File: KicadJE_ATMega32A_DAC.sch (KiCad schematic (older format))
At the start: 97 parts

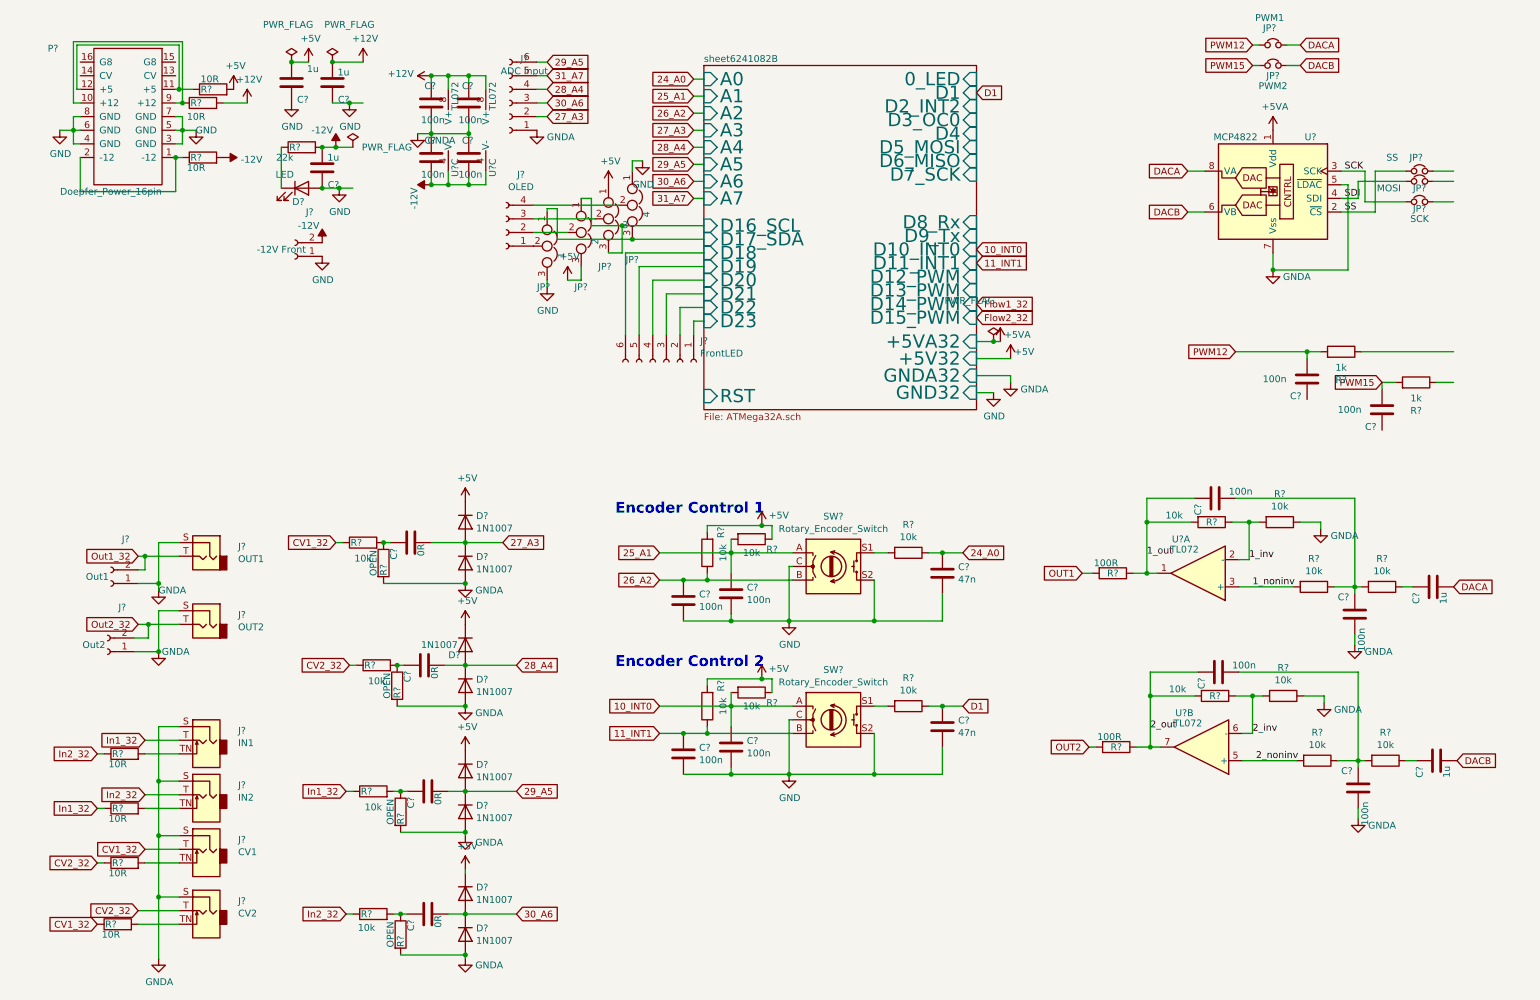
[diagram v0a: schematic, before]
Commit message: annotate dac
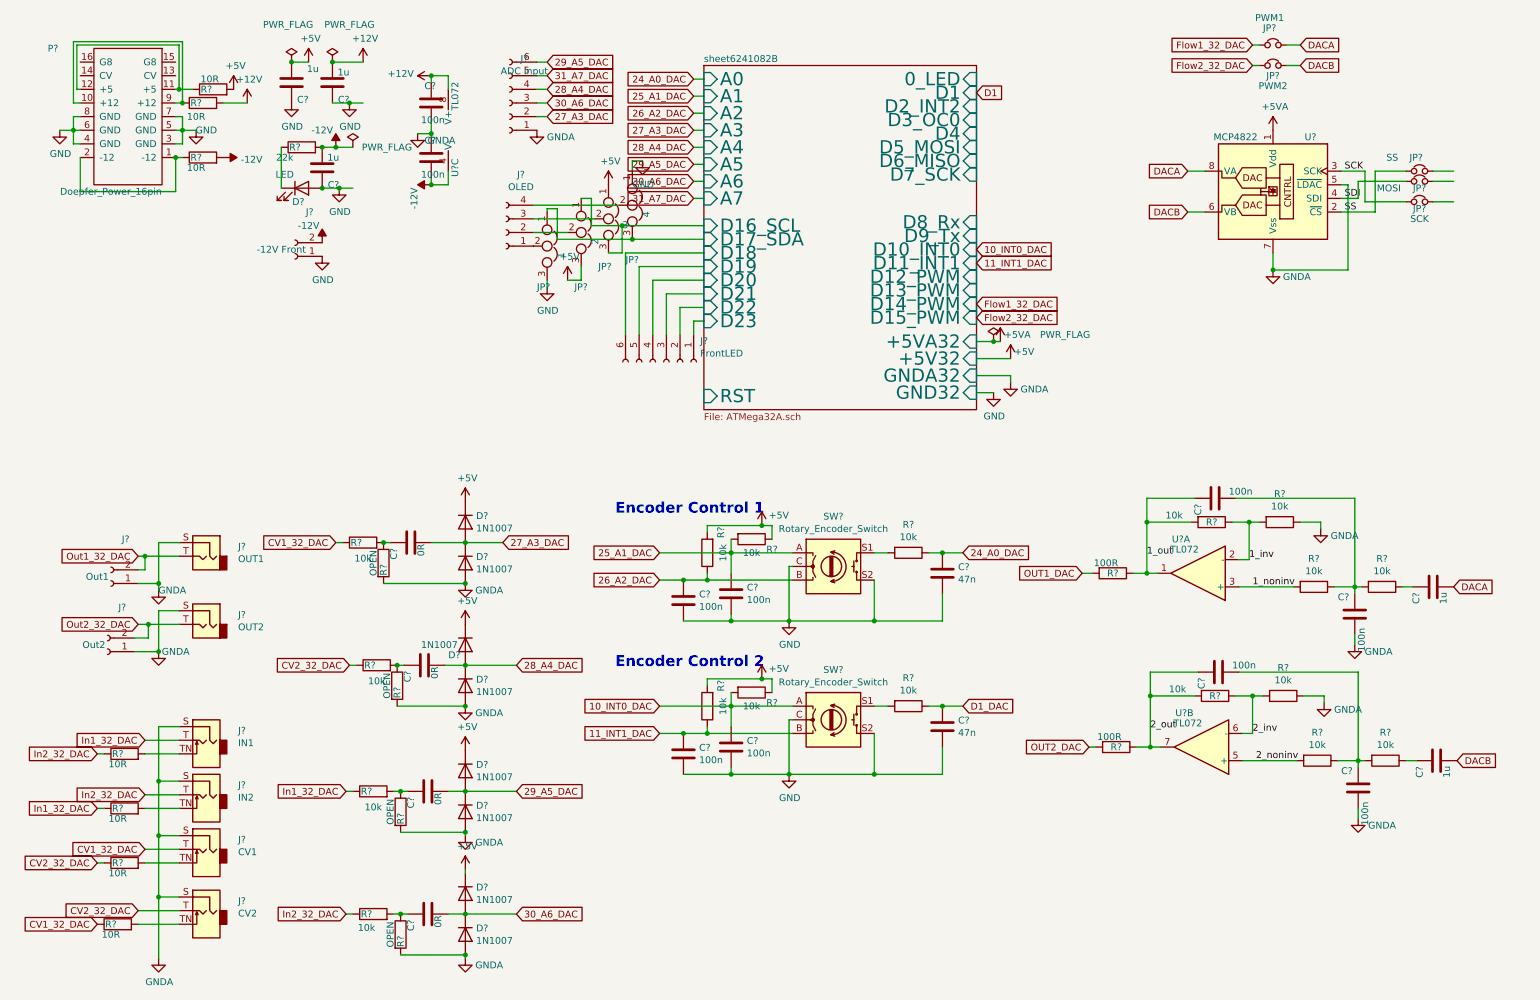
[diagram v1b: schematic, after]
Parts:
- removed C212, C213: 100n, Capacitor_SMD:C_0805_2012Metric_Pad1.15x1.40mm_HandSolder, symbol Device:C
- removed C? (x2): 100n, AJ:C_0805_AJ, symbol Device:C
- removed R218, R223: 1k, Resistor_SMD:R_0805_2012Metric_Pad1.15x1.40mm_HandSolder, symbol Device:R
- removed U?: TL072, AJ:AJ_SO-8_5.3x6.2mm_P1.27mm, symbol Amplifier_Operational:TL072
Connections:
- net D1: no longer C?.1, R?.1
- net 10_INT0 renamed 10_INT0_DAC
- net 11_INT1 renamed 11_INT1_DAC
- net 24_A0 renamed 24_A0_DAC
- net 25_A1 renamed 25_A1_DAC
- net 26_A2 renamed 26_A2_DAC
- net 27_A3 renamed 27_A3_DAC
- net 28_A4 renamed 28_A4_DAC
- net 29_A5 renamed 29_A5_DAC
- net 30_A6 renamed 30_A6_DAC
- net 31_A7 renamed 31_A7_DAC
- net CV1_32 renamed CV1_32_DAC
- net CV2_32 renamed CV2_32_DAC
- net In1_32 renamed In1_32_DAC
- net In2_32 renamed In2_32_DAC
- net OUT1 renamed OUT1_DAC
- net OUT2 renamed OUT2_DAC
- net Out1_32 renamed Out1_32_DAC
- net Out2_32 renamed Out2_32_DAC
- net PWM12 renamed Flow1_32_DAC
- net PWM15 renamed Flow2_32_DAC
- new net D1_DAC: C?.1, R?.1

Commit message: footprints dac
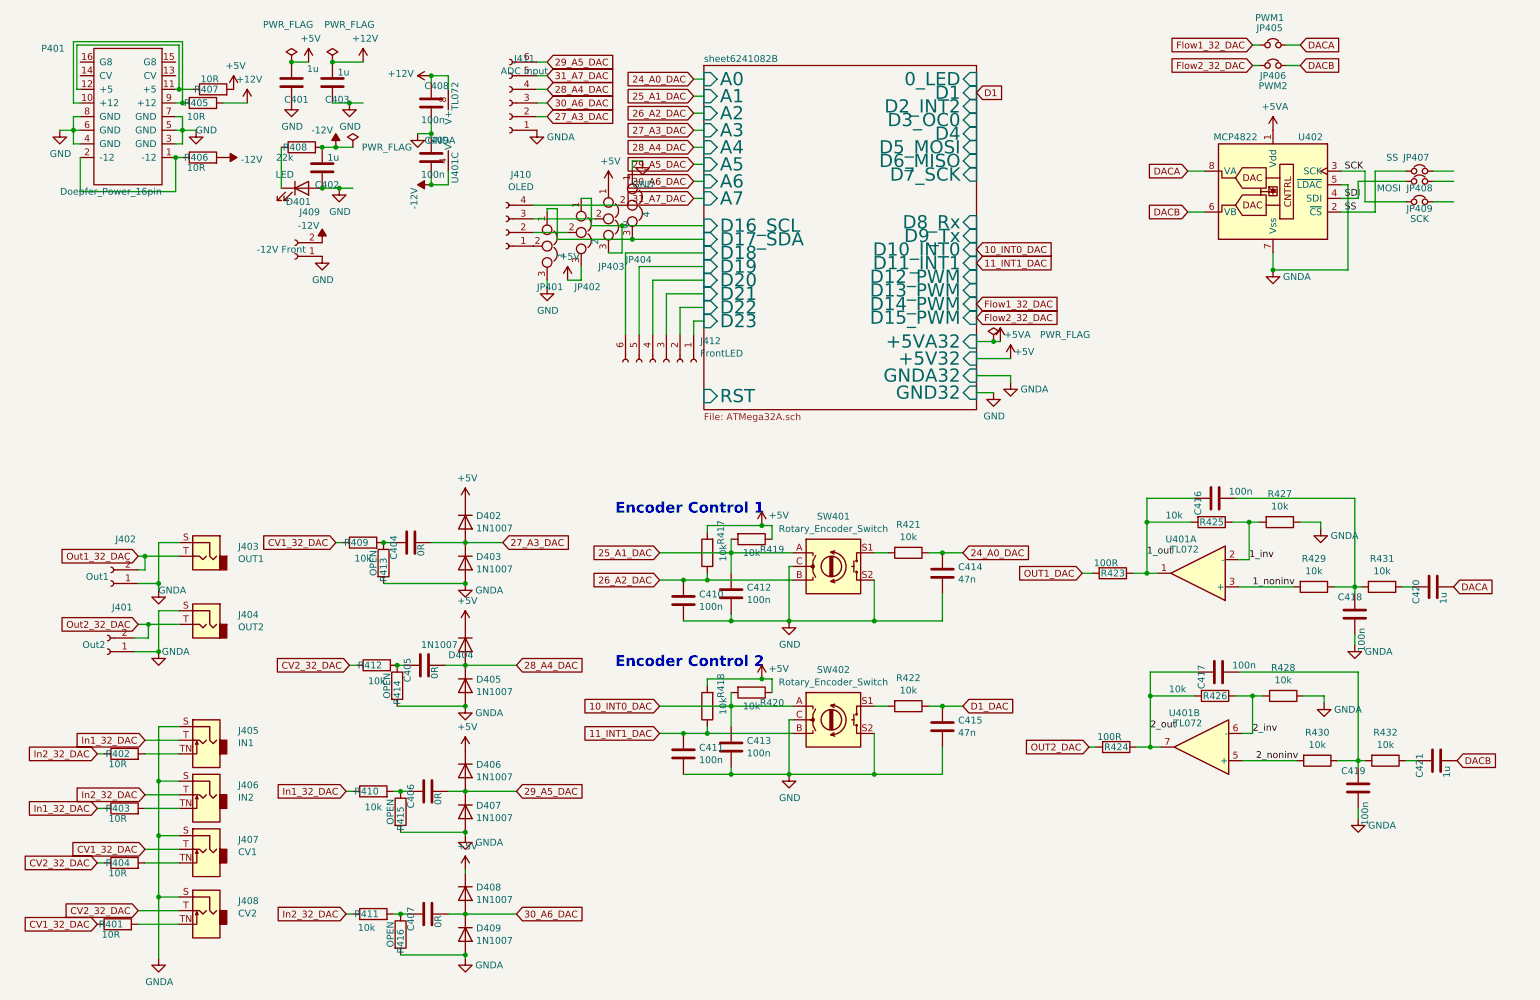
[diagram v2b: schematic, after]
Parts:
- C206, C208, C209, C211: footprint Capacitor_SMD:C_0805_2012Metric_Pad1.15x1.40mm_HandSolder -> AJ:C_0805_AJ
- C207, C210: footprint Capacitor_SMD:C_1206_3216Metric_Pad1.42x1.75mm_HandSolder -> AJ:C_0805_AJ
- R205, R206, R207, R208, R209, R211, R212, R213, R214, R215: footprint Resistor_SMD:R_0805_2012Metric_Pad1.15x1.40mm_HandSolder -> AJ:R_0805_AJ
- gave numbers to parts that had none: 72

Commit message: Components placed
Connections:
- net Out1_32_DAC is gone; now on net OUT1_DAC: J402.2 (Pin_2), J403.T
- net Out2_32_DAC is gone; now on net OUT2_DAC: J401.2 (Pin_2), J404.T
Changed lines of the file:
@@
 Wire Wire Line
 	1200 4975 1275 4975
-Text GLabel 1200 4475 0    50   Input ~ 0
-Out1_32_DAC
-Text GLabel 1200 4975 0    50   Input ~ 0
-Out2_32_DAC
 $Comp
 L power:GNDA #PWR?
@@
 Text GLabel 9375 875  0    50   Input ~ 0
 Flow2_32_DAC
+Text GLabel 1200 4475 0    50   Input ~ 0
+OUT1_DAC
+Text GLabel 1200 4975 0    50   Input ~ 0
+OUT2_DAC
 $EndSCHEMATC

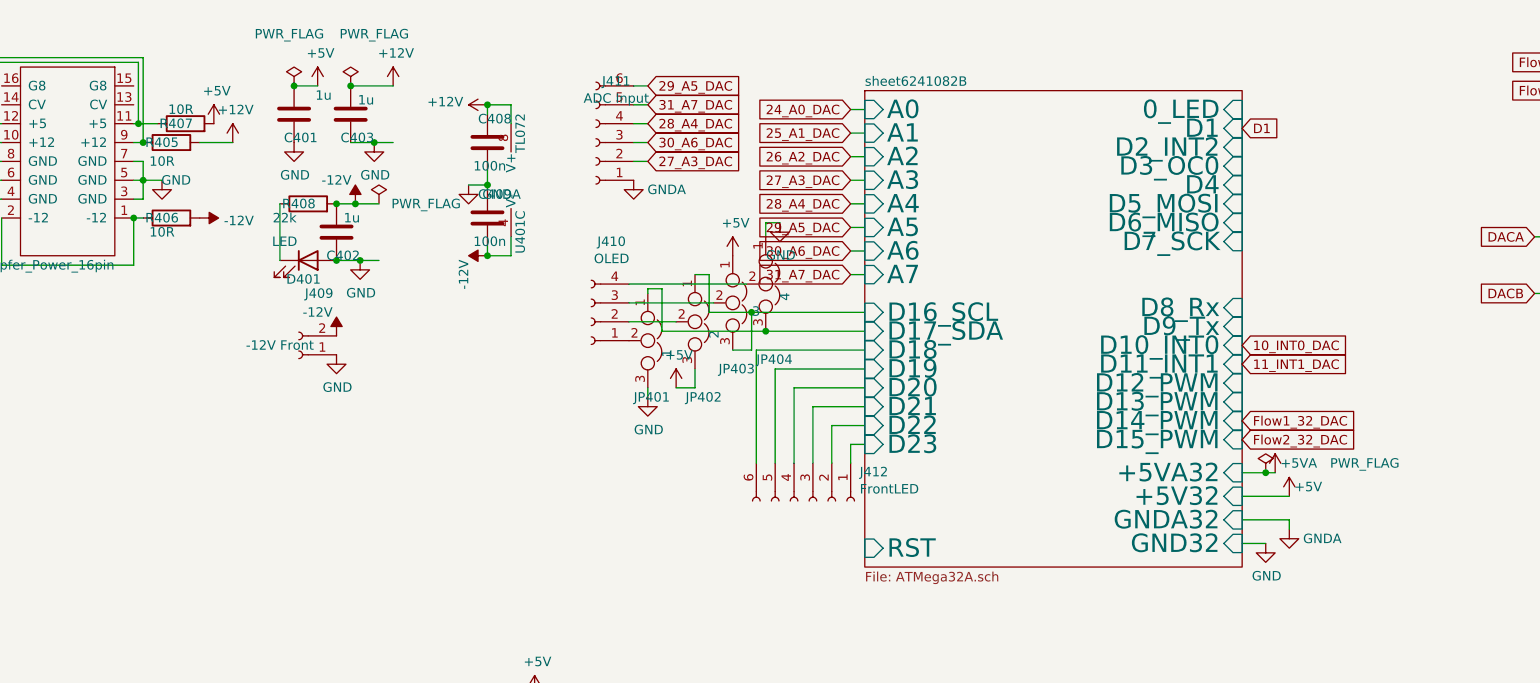
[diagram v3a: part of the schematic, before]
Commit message: Wiring DAC board - initiated
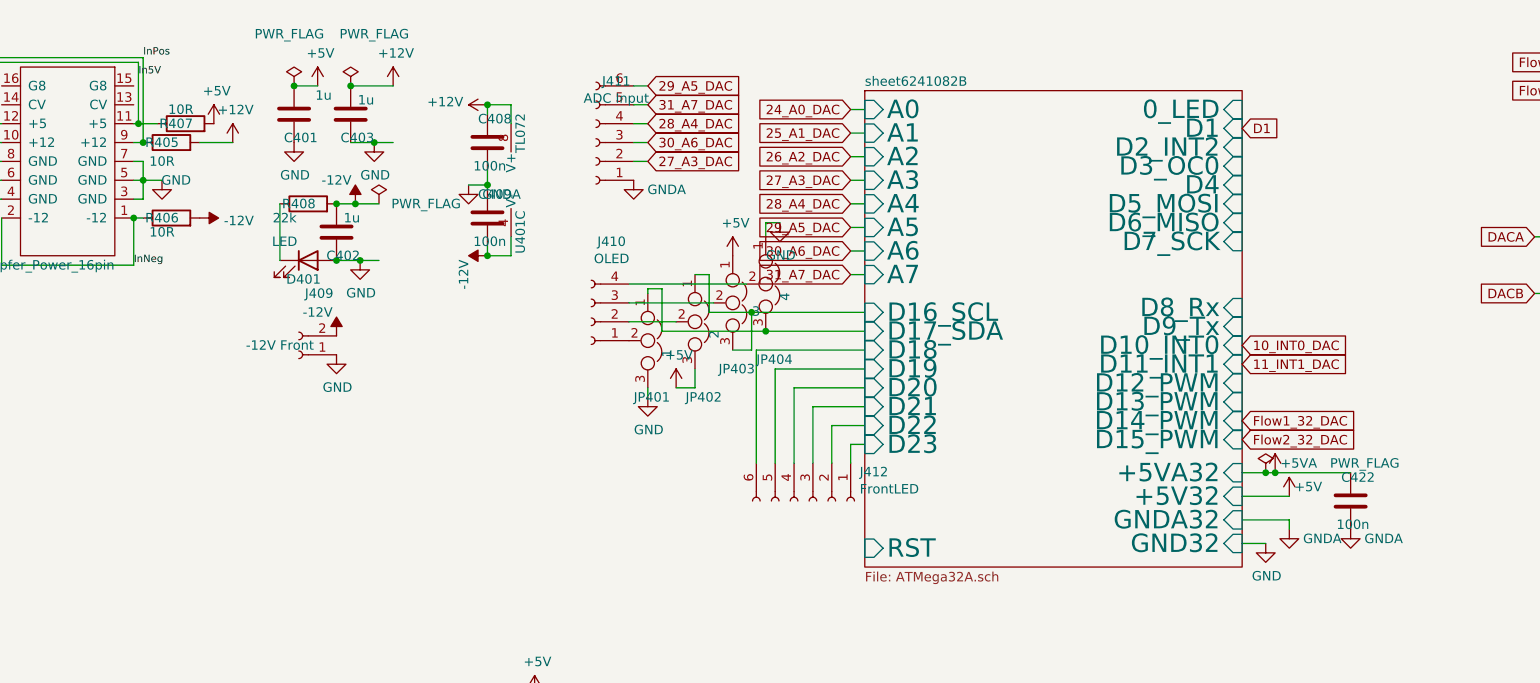
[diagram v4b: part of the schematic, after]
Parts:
- added C422: 100n, AJ:C_0805_AJ, symbol Device:C
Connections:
- net +5VA: now also C422.1
- net GNDA: now also C422.2
- net InNeg: now reaches P401.1 (-12), P401.2 (-12), R406.1
- net InPos: now reaches P401.10 (+12), P401.9 (+12), R405.1
- net In5V: now reaches P401.11 (+5), P401.12 (+5), R407.1
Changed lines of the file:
@@
 Text GLabel 1200 4975 0    50   Input ~ 0
 OUT2_DAC
+Text Label 1475 1800 0    39   ~ 0
+InNeg
+Text Label 1525 700  0    39   ~ 0
+InPos
+Text Label 1500 800  0    39   ~ 0
+In5V
+$Comp
+L Device:C C?
+U 1 1 60B091A5
+P 7925 3050
+AR Path="/5E4B0DD9/60B091A5" Ref="C?"  Part="1"
+AR Path="/5E62ACA1/60B091A5" Ref="C?"  Part="1"
+AR Path="/5F49A670/60B091A5" Ref="C?"  Part="1"
+AR Path="/60B091A5" Ref="C?"  Part="1"
+AR Path="/608CA457/60B091A5" Ref="C?"  Part="1"
+AR Path="/623B09EB/60B091A5" Ref="C422"  Part="1"
+F 0 "C422" H 7875 3175 50  0000 L CNN
+F 1 "100n" H 7850 2925 50  0000 L CNN
+F 2 "AJ:C_0805_AJ" H 7963 2900 50  0001 C CNN
+F 3 "~" H 7925 3050 50  0001 C CNN
+	1    7925 3050
+	1    0    0    -1
+$EndComp
+$Comp
+L power:GNDA #PWR?
+U 1 1 60B44143
+P 7925 3200
+AR Path="/60B44143" Ref="#PWR?"  Part="1"
+AR Path="/5CD3F059/60B44143" Ref="#PWR?"  Part="1"
+AR Path="/608CA457/60B44143" Ref="#PWR?"  Part="1"
+AR Path="/623B09EB/60B44143" Ref="#PWR?"  Part="1"
+F 0 "#PWR?" H 7925 2950 50  0001 C CNN
+F 1 "GNDA" H 8100 3150 50  0000 C CNN
+F 2 "" H 7925 3200 50  0001 C CNN
+F 3 "" H 7925 3200 50  0001 C CNN
+	1    7925 3200
+	1    0    0    -1
+$EndComp
+Wire Wire Line
+	7525 2900 7925 2900
+Connection ~ 7525 2900
 $EndSCHEMATC

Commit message: Update KicadJE_ATMega32A_DAC.sch
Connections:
- net SCK_DAC: now reaches JP409.2
- net MOSI_DAC: now reaches JP408.2
- net CS_DAC: now reaches JP407.2
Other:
- moved on the sheet: JP407, JP409
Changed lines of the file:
@@
 L Device:Jumper_NC_Small JP409
 U 1 1 5CF0FB40
-P 10600 1875
-F 0 "JP409" H 10600 1825 50  0000 C CNN
-F 1 "SCK" H 10600 1750 50  0000 C CNN
-F 2 "Connector_PinSocket_2.54mm:PinSocket_1x02_P2.54mm_Vertical" H 10600 1875 50  0001 C CNN
-F 3 "~" H 10600 1875 50  0001 C CNN
-	1    10600 1875
+P 10600 1650
+F 0 "JP409" H 10725 1700 50  0000 C CNN
+F 1 "SCK" H 10425 1675 50  0000 C CNN
+F 2 "Connector_PinSocket_2.54mm:PinSocket_1x02_P2.54mm_Vertical" H 10600 1650 50  0001 C CNN
+F 3 "~" H 10600 1650 50  0001 C CNN
+	1    10600 1650
 	1    0    0    -1
 $EndComp
@@
 U 1 1 5CF100A7
 P 10600 1725
-F 0 "JP408" H 10600 1675 50  0000 C CNN
-F 1 "MOSI" H 10375 1675 50  0000 C CNN
+F 0 "JP408" H 10775 1675 50  0000 C CNN
+F 1 "MOSI" H 10350 1725 50  0000 C CNN
 F 2 "Connector_PinSocket_2.54mm:PinSocket_1x02_P2.54mm_Vertical" H 10600 1725 50  0001 C CNN
 F 3 "~" H 10600 1725 50  0001 C CNN
@@
 L Device:Jumper_NC_Small JP407
 U 1 1 5CF10382
-P 10600 1650
-F 0 "JP407" H 10575 1750 50  0000 C CNN
-F 1 "SS" H 10400 1750 50  0000 C CNN
-F 2 "Connector_PinSocket_2.54mm:PinSocket_1x02_P2.54mm_Vertical" H 10600 1650 50  0001 C CNN
-F 3 "~" H 10600 1650 50  0001 C CNN
-	1    10600 1650
-	1    0    0    -1
-$EndComp
+P 10600 1950
+F 0 "JP407" H 10675 1900 50  0000 C CNN
+F 1 "SS" H 10425 2000 50  0000 C CNN
+F 2 "Connector_PinSocket_2.54mm:PinSocket_1x02_P2.54mm_Vertical" H 10600 1950 50  0001 C CNN
+F 3 "~" H 10600 1950 50  0001 C CNN
+	1    10600 1950
+	1    0    0    -1
+$EndComp
+Wire Wire Line
+	10700 1950 10850 1950
+Wire Wire Line
+	10700 1725 10850 1725
 Wire Wire Line
 	10700 1650 10850 1650
-Wire Wire Line
-	10700 1725 10850 1725
-Wire Wire Line
-	10700 1875 10850 1875
-Wire Wire Line
-	10500 1875 10200 1875
-Wire Wire Line
-	10200 1875 10200 1650
-Wire Wire Line
-	10200 1650 10025 1650
-Wire Wire Line
-	10500 1650 10275 1650
-Wire Wire Line
-	10275 1650 10275 1950
-Wire Wire Line
-	10275 1950 10025 1950
 Wire Wire Line
 	10500 1725 10150 1725
@@
 AR Path="/5CD3F059/60B44143" Ref="#PWR?"  Part="1"
 AR Path="/608CA457/60B44143" Ref="#PWR?"  Part="1"
-AR Path="/623B09EB/60B44143" Ref="#PWR?"  Part="1"
-F 0 "#PWR?" H 7925 2950 50  0001 C CNN
+AR Path="/623B09EB/60B44143" Ref="#PWR0154"  Part="1"
+F 0 "#PWR0154" H 7925 2950 50  0001 C CNN
 F 1 "GNDA" H 8100 3150 50  0000 C CNN
 F 2 "" H 7925 3200 50  0001 C CNN
@@
 	7525 2900 7925 2900
 Connection ~ 7525 2900
+Text GLabel 10850 1950 2    50   Input ~ 0
+CS_DAC
+Text GLabel 7350 1675 2    50   Input ~ 0
+SCK_DAC
+Text GLabel 10850 1725 2    50   Input ~ 0
+MOSI_DAC
+Text GLabel 10850 1650 2    50   Input ~ 0
+SCK_DAC
+Text GLabel 7350 1475 2    50   Input ~ 0
+MOSI_DAC
+Text GLabel 7350 1375 2    50   Input ~ 0
+CS_DAC
+Wire Wire Line
+	10025 1950 10500 1950
+Wire Wire Line
+	10025 1650 10500 1650
 $EndSCHEMATC

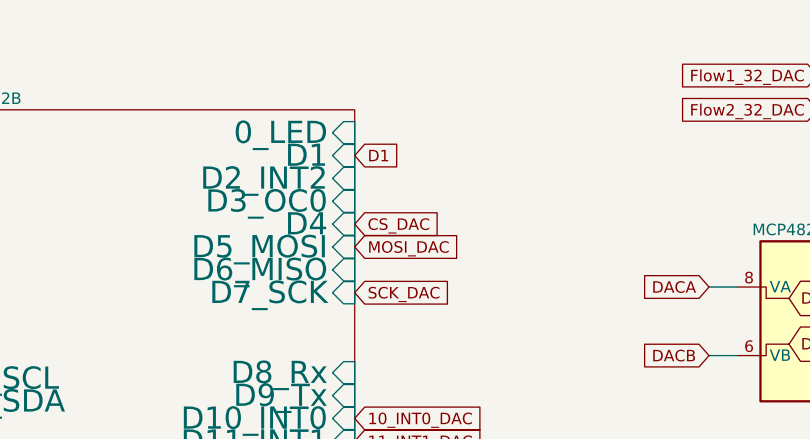
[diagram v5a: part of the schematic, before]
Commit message: D1 -> D1_DAC
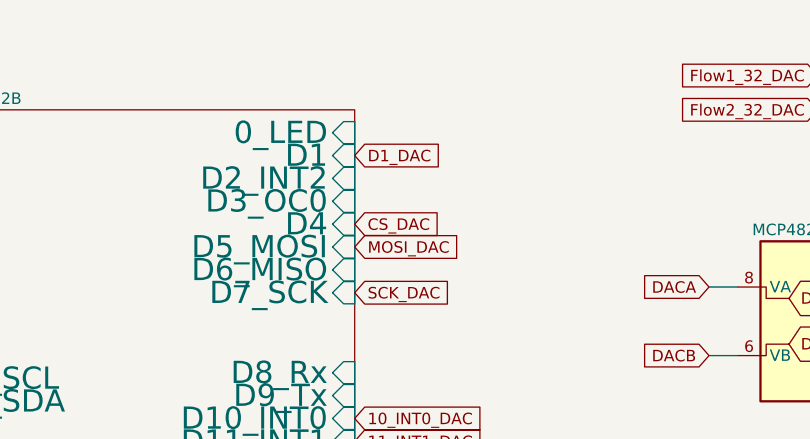
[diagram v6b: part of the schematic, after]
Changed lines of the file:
@@
 Text GLabel 7350 2325 2    50   Input ~ 0
 11_INT1_DAC
-Text GLabel 7350 1075 2    50   Input ~ 0
-D1
 Text GLabel 4200 850  2    50   Input ~ 0
 29_A5_DAC
@@
 Wire Wire Line
 	10025 1650 10500 1650
+Text GLabel 7350 1075 2    50   Input ~ 0
+D1_DAC
 $EndSCHEMATC
